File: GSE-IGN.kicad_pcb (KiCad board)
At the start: 2 copper layers, 99.1 x 99.1 mm, 39 parts, among them J1 Conn_01x02, J2 DCDC-Regulator-12Vto3.3V, J3 debug-sw1, J4 RJ45, J5 Igniter-1, J6 debug-sw1, J7 Igniter-2, Q1 BSS138, U1 Pico, U3 TLP3543A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

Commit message: schはたぶん完成
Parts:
- added C2: 0.1uF, Capacitor_SMD:C_01005_0402Metric, F.Cu at (44.8, 80.9)
- added C3: 0.1u, Capacitor_SMD:C_0402_1005Metric, F.Cu at (65.1, 67.8)
- added C4: 10u, Capacitor_THT:CP_Radial_D4.0mm_P1.50mm, F.Cu at (65.7, 64.1)
- added J8: RJ45, Connector_RJ:RJ45_Wuerth_7499010211A_Horizontal, F.Cu at (49.2, 59.8)
- added J9: Conn_01x04_Socket, Connector_PinSocket_1.00mm:PinSocket_1x04_P1.00mm_Vertical, F.Cu at (65.7, 56.5)
- C1: value 10u -> 0.1u; footprint Capacitor_SMD:C_0805_2012Metric_Pad1.18x1.45mm_HandSolder -> Diode_SMD:D_0402_1005Metric
- C7: footprint Capacitor_SMD:C_0805_2012Metric_Pad1.18x1.45mm_HandSolder -> Capacitor_THT:CP_Radial_D5.0mm_P2.00mm
- D1: footprint Diode_THT:D_DO-41_SOD81_P12.70mm_Horizontal -> 0000_my_footprint:SBM1060LSS_P20mm_Horizontal
- J2: value DCDC-Regulator-12Vto3.3V -> LD1117S50; footprint Connector_PinSocket_2.54mm:PinSocket_1x03_P2.54mm_Horizontal -> Package_TO_SOT_SMD:SOT-223-3_TabPin2
- R11, R12: value ? -> 1k
- R3: value 240 -> 500
- U1: value Pico -> ATMEGA328P-PU; footprint KiCad-RP-Pico-main:RPi_Pico_SMD_TH -> Package_DIP:DIP-28_W7.62mm
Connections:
- D3 pad 1: Net-(D3-K) -> +12V
- D3 pad 2: GND -> Net-(D3-A)
- D4 pad 2: +3.3V -> +5V
- D5 pad 1: GND -> Net-(D3-A)
- D7 pad 1: GND -> Net-(D7-K)
- D8 pad 1: Net-(D8-K) -> +12V
- D8 pad 2: GND -> Net-(D7-K)
- J2 pad 1: +3.3V -> GND
- J2 pad 2: GND -> +5V
- J4 pad 3: /RS485/B -> unconnected-(J4-Pad3)
- J4 pad 4: GND -> /RS485/B
- J4 pad 5: GND -> /RS485/A
- J4 pad 6: /RS485/A -> unconnected-(J4-Pad6)
- J5 pad 1: GND -> Net-(D3-A)
- J5 pad 2: Net-(D3-K) -> +12V
- J7 pad 1: GND -> Net-(D7-K)
- J7 pad 2: Net-(D8-K) -> +12V
- JP1 pad 2: +3.3V -> +5V
- R11 pad 1: /RS485/RS485_*RE -> /RS485_*RE
- R12 pad 1: /RS232C-TX-IN -> /RS485_DE
- R3 pad 2: +3.3V -> +5V
- R5 pad 2: Net-(D3-K) -> +12V
- R7 pad 2: +3.3V -> +5V
- R8 pad 2: +3.3V -> +5V
- R9 pad 2: Net-(D8-K) -> +12V
- U1 pad 1: /RS232C-TX-IN -> Net-(J9-Pin_4)
- U1 pad 11: unconnected-(U1-GPIO8-Pad11)_1 -> /Debug-sw1
- U1 pad 12: unconnected-(U1-GPIO9-Pad12)_1 -> /Debug-sw2
- U1 pad 13: GND -> unconnected-(U1-PD7-Pad13)
- U1 pad 14: /Igniter-signal -> unconnected-(U1-PB0-Pad14)
- U1 pad 15: unconnected-(U1-GPIO11-Pad15)_1 -> Net-(J9-Pin_1)
- U1 pad 16: unconnected-(U1-GPIO12-Pad16)_1 -> Net-(J9-Pin_2)
- U1 pad 17: unconnected-(U1-GPIO13-Pad17)_1 -> Net-(J9-Pin_3)
- U1 pad 18: GND -> unconnected-(U1-PB4-Pad18)
- U1 pad 20: unconnected-(U1-GPIO15-Pad20) -> Net-(D4-K)
- U1 pad 22: unconnected-(U1-GPIO17-Pad22) -> GND
- U1 pad 23: GND -> unconnected-(U1-PC0-Pad23)
- U1 pad 28: GND -> unconnected-(U1-PC5-Pad28)
- U1 pad 3: GND -> /RS232C-TX-IN
- U1 pad 4: /Debug-sw1 -> /RS485_DE
- U1 pad 5: /Debug-sw2 -> /RS485_*RE
- U1 pad 6: unconnected-(U1-GPIO4-Pad6) -> /Igniter-signal
- U1 pad 7: unconnected-(U1-GPIO5-Pad7) -> Net-(D4-K)
- U3 pad 4: Net-(D8-K) -> Net-(D7-K)
- U3 pad 5: Net-(D3-K) -> GND
- U3 pad 6: +12V -> Net-(D3-A)
- U4 pad 2: /RS485/RS485_*RE -> /RS485_*RE
- U4 pad 3: /RS232C-TX-IN -> /RS485_DE
- U4 pad 4: /RS485/RS485_TX_IN -> /RS232C-TX-IN
- U4 pad 8: +3.3V -> +5V
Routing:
- net +5V: track 0.00 -> 94.6 mm
- net +3.3V: track 94.6 -> 0.00 mm

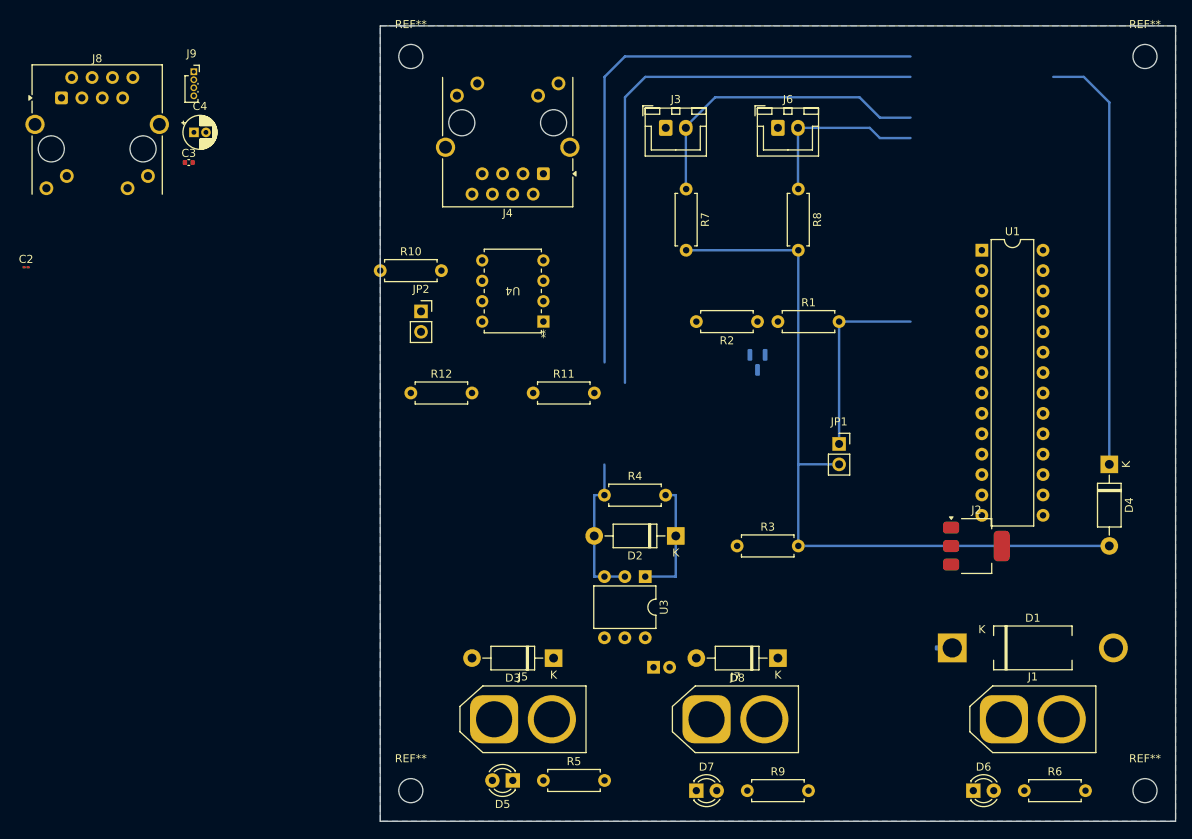
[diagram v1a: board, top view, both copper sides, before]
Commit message: 部品を配置
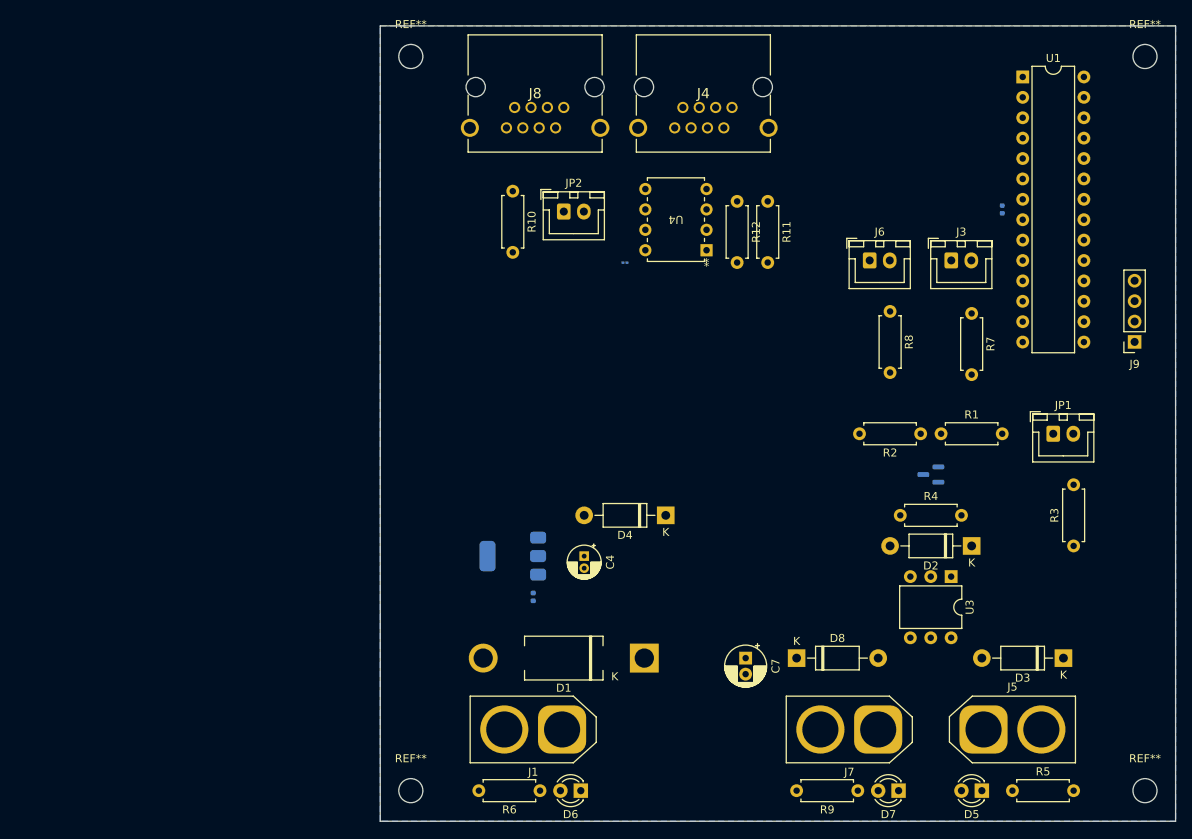
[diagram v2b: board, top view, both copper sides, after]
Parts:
- C2, C3, J2: moved to B.Cu
- C7: moved to F.Cu
- J4, J8: footprint Connector_RJ:RJ45_Wuerth_7499010211A_Horizontal -> 0000_my_footprint:78108P8C
- J9: footprint Connector_PinSocket_1.00mm:PinSocket_1x04_P1.00mm_Vertical -> Connector_PinSocket_2.54mm:PinSocket_1x04_P2.54mm_Vertical
- JP1, JP2: footprint Connector_PinSocket_2.54mm:PinSocket_1x02_P2.54mm_Vertical -> Connector_JST:JST_XH_B2B-XH-A_1x02_P2.50mm_Vertical
- moved J9 121.9 mm to (182.9, 90.2), turned to 180 degrees
- moved C3 101.5 mm to (166.4, 73.7), turned to -90 degrees
- moved C2 74.6 mm to (119.4, 80.3), turned to 180 degrees
- moved C4 71.8 mm to (114.3, 116.8), turned to -90 degrees
- moved D3 63.5 mm to (174.0, 129.5)
- moved J8 62.6 mm to (111.8, 61.0), turned to 180 degrees
- moved J5 61.0 mm to (164.0, 138.4)
- moved R6 60.3 mm to (108.8, 146.1), turned to 180 degrees
- moved D5 58.4 mm to (163.8, 146.1)
- moved R5 58.4 mm to (167.6, 146.1)
- moved J2 57.8 mm to (105.4, 116.8), turned to 180 degrees
- moved D4 55.6 mm to (124.5, 111.8), turned to 180 degrees
- moved J1 55.0 mm to (111.5, 138.4), turned to 180 degrees
- moved C1 51.2 mm to (108.0, 121.9), turned to -90 degrees
- moved D6 48.9 mm to (113.9, 146.1), turned to 180 degrees
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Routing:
- net +5V: track 94.6 -> 0.00 mm
- net /RS232C-TX-IN: track 74.7 -> 0.00 mm
- net /RS232C-RX-OUT: track 72.2 -> 0.00 mm
- net Net-(D4-K): track 53.4 -> 0.00 mm
- net /Debug-sw1: track 38.3 -> 0.00 mm
- net /Igniter-signal: track 24.1 -> 0.00 mm
- net /Debug-sw2: track 22.2 -> 0.00 mm
- net Net-(D2-A): track 19.1 -> 0.00 mm
- net Net-(D2-K): track 15.2 -> 0.00 mm

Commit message: アートワーク終わり
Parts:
- added C5: 22p, Capacitor_SMD:C_0603_1608Metric, B.Cu at (160.1, 83.8)
- added C6: 22p, Capacitor_SMD:C_0603_1608Metric, B.Cu at (165.1, 83.8)
- added Y1: Crystal_GND3_Small, Crystal:Crystal_HC49-4H_Vertical, F.Cu at (165.0, 81.3)
- C1: value 0.1u -> 10u; footprint Diode_SMD:D_0402_1005Metric -> Capacitor_THT:CP_Radial_D4.0mm_P1.50mm; moved to F.Cu
- C2: footprint Capacitor_SMD:C_01005_0402Metric -> Capacitor_SMD:C_0402_1005Metric
- moved D4 40.5 mm to (154.9, 85.1), turned to -90 degrees
- moved J9 33.6 mm to (176.5, 57.2), turned to -90 degrees
- moved J6 30.5 mm to (180.3, 78.8), turned to -90 degrees
- moved U1 26.8 mm to (146.1, 71.1), turned to 90 degrees
- moved R8 25.4 mm to (177.8, 86.4)
- moved R3 15.9 mm to (162.6, 106.0)
- moved C1 13.6 mm to (121.3, 119.4), turned to 0 degrees
- moved J3 12.8 mm to (172.7, 78.8), turned to -90 degrees
- moved R10 12.6 mm to (107.6, 83.8), turned to 90 degrees
- moved R7 12.1 mm to (174.6, 86.4)
- moved R11 9.59 mm to (133.0, 81.3)
- moved J2 8.98 mm to (114.3, 115.6)
- moved R1 8.03 mm to (151.1, 104.1)
- moved R2 8.03 mm to (148.6, 104.1)
- moved C4 7.43 mm to (121.3, 114.3), turned to 0 degrees
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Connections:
- J4 pad 5: /RS485/A -> unconnected-(J4-Pad5)
- J4 pad 6: unconnected-(J4-Pad6) -> /RS485/A
- J8 pad 5: /RS485/A -> unconnected-(J8-Pad5)
- J8 pad 6: unconnected-(J8-Pad6) -> /RS485/A
- JP1 pad 1: /Igniter-signal -> +5V
- JP1 pad 2: +5V -> /Igniter-signal
- JP2 pad 1: /RS485/B -> Net-(JP2-A)
- JP2 pad 2: Net-(JP2-B) -> /RS485/B
- R10 pad 1: Net-(JP2-B) -> Net-(JP2-A)
- U1 pad 10: unconnected-(U1-XTAL2/PB7-Pad10) -> Net-(U1-XTAL2/PB7)
- U1 pad 9: unconnected-(U1-XTAL1/PB6-Pad9) -> Net-(U1-XTAL1/PB6)
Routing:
- net +12V: track 0.00 -> 117.0 mm
- net +5V: track 0.00 -> 107.6 mm
- net /RS485/B: track 0.00 -> 106.2 mm
- net /RS485/A: track 0.00 -> 105.8 mm
- net /Igniter-signal: track 0.00 -> 81.0 mm
- net Net-(J9-Pin_4): track 0.00 -> 37.4 mm
- net /RS232C-RX-OUT: track 0.00 -> 33.5 mm
- net /RS232C-TX-IN: track 0.00 -> 33.4 mm
- net /RS485_*RE: track 0.00 -> 32.8 mm
- net /RS485_DE: track 0.00 -> 29.2 mm
- net Net-(D4-K): track 0.00 -> 26.3 mm
- net /Debug-sw2: track 0.00 -> 19.7 mm
- net Net-(D1-A): track 0.00 -> 18.9 mm
- net /Debug-sw1: track 0.00 -> 18.4 mm
- net Net-(U1-XTAL1/PB6): track 0.00 -> 14.5 mm
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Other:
- outline, holes or cut-outs redrawn

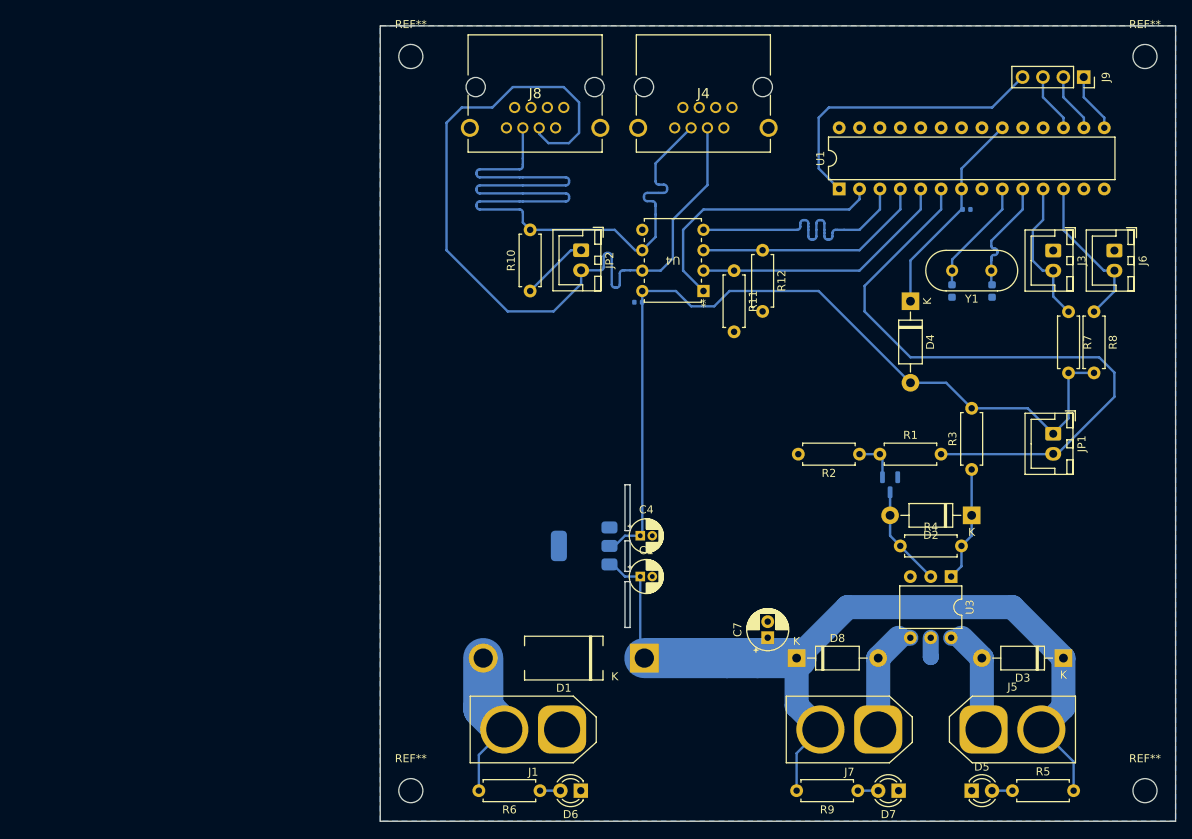
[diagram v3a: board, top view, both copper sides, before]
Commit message: 少し小型化
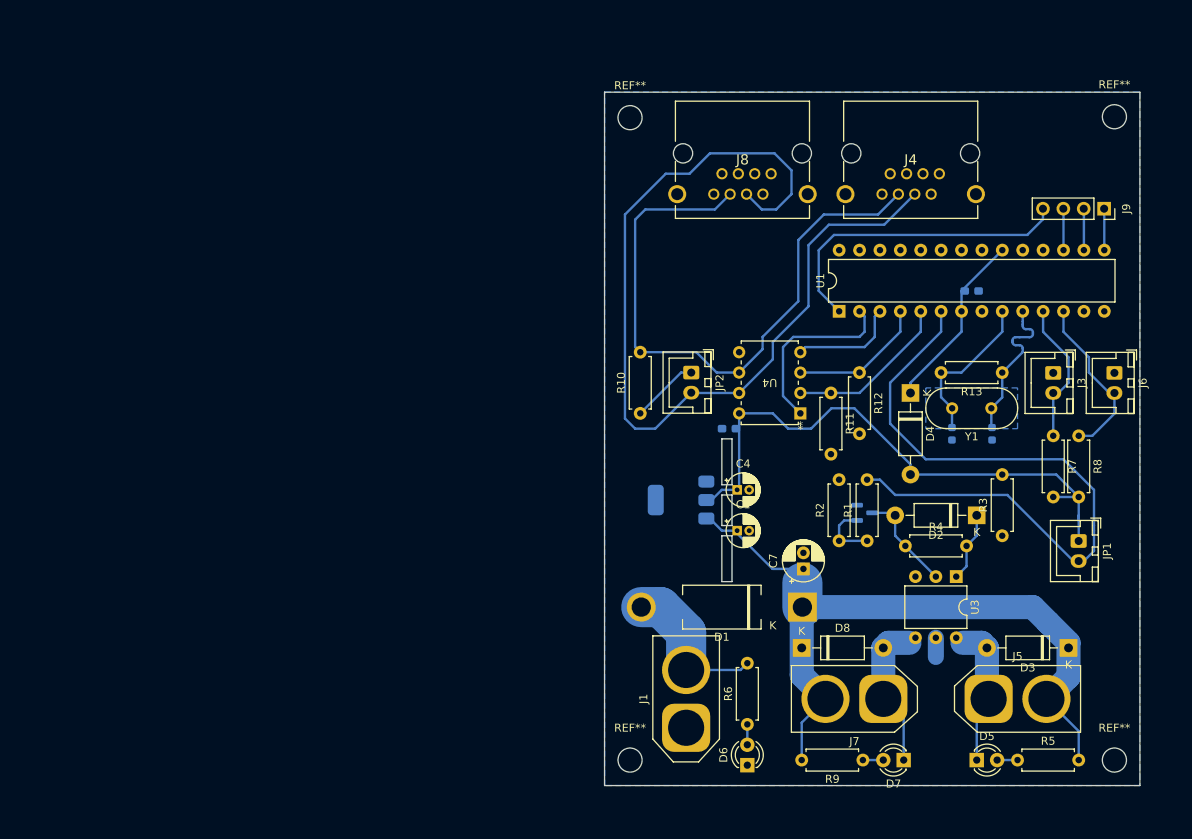
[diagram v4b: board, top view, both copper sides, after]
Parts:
- added R13: 1M, Resistor_THT:R_Axial_DIN0207_L6.3mm_D2.5mm_P7.62mm_Horizontal, F.Cu at (166.4, 94.0)
- C1, C4: value 10u -> 47u
- C2, C3: footprint Capacitor_SMD:C_0402_1005Metric -> Capacitor_SMD:C_0603_1608Metric_Pad1.08x0.95mm_HandSolder
- moved REF** 28.3 mm to (120.0, 62.2)
- moved REF** 27.6 mm to (120.0, 142.2)
- moved J4 27.1 mm to (158.5, 69.2)
- moved J8 27.1 mm to (137.6, 69.2)
- moved R6 27.1 mm to (134.6, 137.8), turned to 90 degrees
- moved D6 21.0 mm to (134.6, 142.9), turned to 90 degrees
- moved D1 20.7 mm to (137.8, 123.2)
- moved JP2 20.5 mm to (127.6, 94.0)
- moved R10 20.5 mm to (121.3, 99.1)
- moved R12 19.4 mm to (148.6, 94.0)
- moved U4 19.4 mm to (141.2, 99.1)
- moved R11 19.4 mm to (145.0, 96.5)
- moved C2 19.4 mm to (132.3, 101.0)
- moved C5 17.8 mm to (160.1, 101.6)
- moved C6 17.8 mm to (165.1, 101.6)
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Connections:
- J8 pad 10: (no net) -> GND
- J8 pad 9: (no net) -> GND
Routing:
- net +5V: track 107.6 -> 73.7 mm
- net /RS485/A: track 105.8 -> 77.7 mm
- net +12V: track 117.0 -> 92.2 mm
- net /RS232C-TX-IN: track 33.4 -> 13.5 mm
- net /RS485_*RE: track 32.8 -> 20.7 mm
- net /RS485_DE: track 29.2 -> 17.1 mm
- net /RS232C-RX-OUT: track 33.5 -> 22.9 mm
- net /RS485/B: track 106.2 -> 114.9 mm
- net Net-(D2-K): track 14.4 -> 8.69 mm
- net /Igniter-signal: track 81.0 -> 86.7 mm
- net Net-(U1-XTAL2/PB7): track 14.5 -> 20.1 mm
- net Net-(U1-XTAL1/PB6): track 14.5 -> 19.7 mm
- net Net-(D7-K): track 13.9 -> 18.5 mm
- net Net-(D3-A): track 13.8 -> 18.0 mm
- net Net-(D4-K): track 26.3 -> 22.5 mm
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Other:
- board size 99.1 x 99.1 mm -> 66.7 x 86.4 mm
